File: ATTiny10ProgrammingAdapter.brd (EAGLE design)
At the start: 46.7 x 45.7 mm, 9 parts

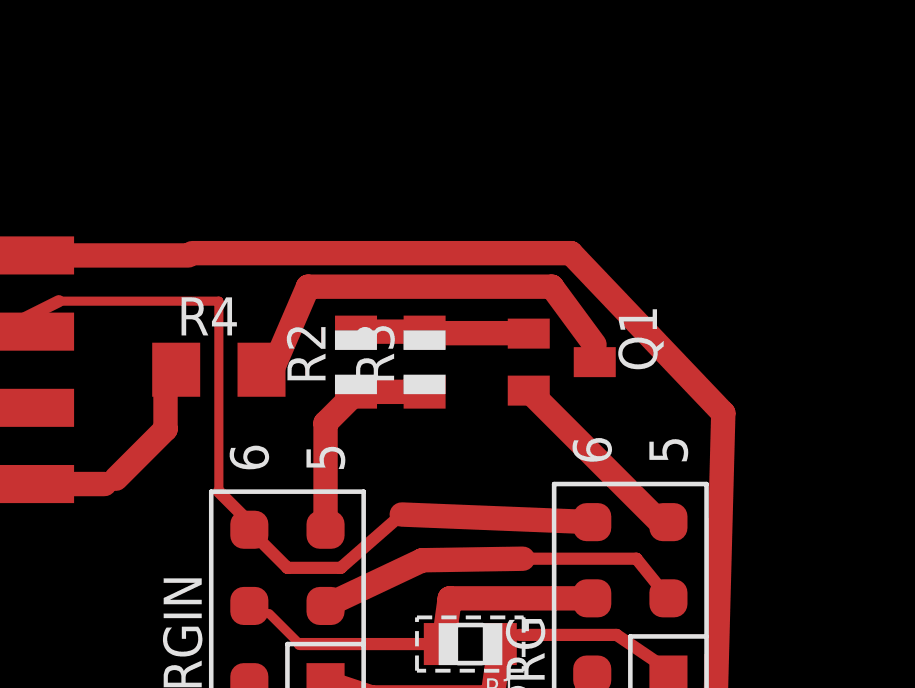
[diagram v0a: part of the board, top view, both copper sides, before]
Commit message: Fix rest to default to pulldown when not active
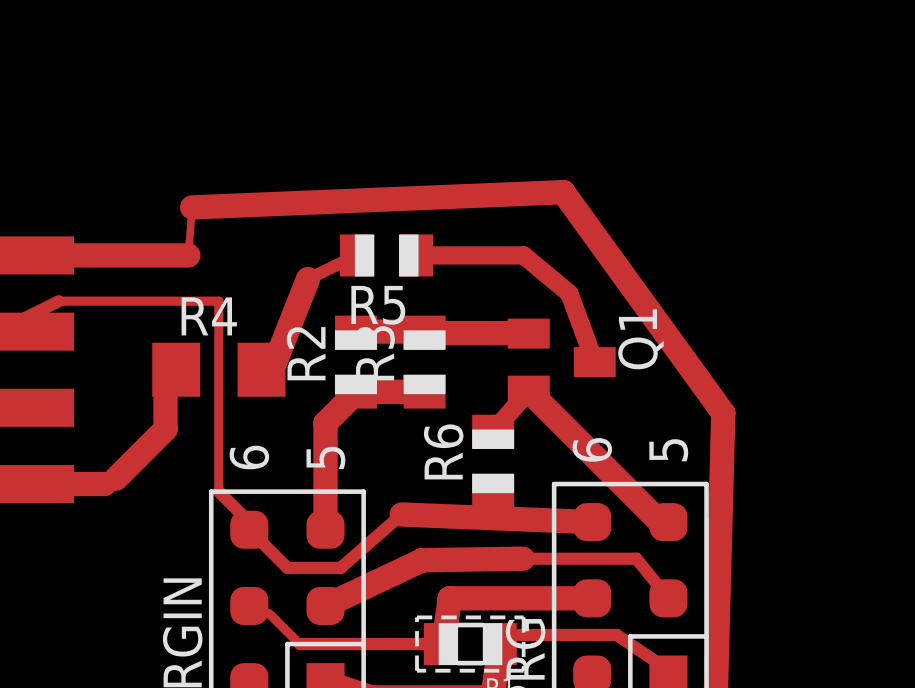
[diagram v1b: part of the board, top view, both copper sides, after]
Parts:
- added R5: 50k, adafruit:R0805
- added R6: 2k, adafruit:R0805
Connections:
- new net N$4: Q1.3, R5.1
- net +12V: now also R5.2; no longer Q1.3
- net GND: now also R6.1
- net RST: now also R6.2
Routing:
- net +12V: track 23.0 -> 13.9 mm
- net N$4: track 0.00 -> 7.99 mm
- net VDD: track 40.7 -> 43.6 mm
- net RST: track 6.47 -> 8.25 mm
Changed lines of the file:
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@@
 <element name="PRGIN" library="LL" package="HEADER_PRG_2X03_ETCH" value="CON_HEADER_PRG_AVR_ICSP_ETCH" x="12.192" y="9.652" rot="R90"/>
 <element name="R4" library="LL" package="R1206" value="0" x="9.906" y="17.526"/>
+<element name="R5" library="adafruit" package="R0805" value="50k" x="15.494" y="21.336" rot="R180"/>
+<element name="R6" library="adafruit" package="R0805" value="2k" x="19.05" y="14.478" rot="R90"/>
 </elements>
 <signals>
 <signal name="RST">
-<contactref element="Q1" pad="2"/>
 <contactref element="PRG" pad="5"/>
 <wire x1="24.6126" y1="12.446" x2="24.892" y2="12.446" width="0.254" layer="1"/>
 <wire x1="20.2438" y1="16.8148" x2="24.6126" y2="12.446" width="0.8128" layer="1"/>
-<wire x1="20.2438" y1="16.8148" x2="20.236" y2="16.83" width="0.254" layer="1"/>
+<contactref element="R6" pad="2"/>
+<contactref element="Q1" pad="2"/>
+<wire x1="20.2438" y1="16.8148" x2="19.05" y2="15.478" width="0.6096" layer="1"/>
+<wire x1="20.2438" y1="16.8148" x2="20.236" y2="16.83" width="0" layer="19" extent="1-1"/>
 </signal>
 <signal name="TPICLK">
@@
 <wire x1="9.906" y1="19.812" x2="4.572" y2="19.812" width="0.3048" layer="1"/>
 <wire x1="4.572" y1="19.812" x2="2.54" y2="18.796" width="0.4064" layer="1"/>
+<contactref element="R6" pad="1"/>
 </signal>
 <signal name="+12V">
 <contactref element="EXTPOWER" pad="4"/>
-<contactref element="Q1" pad="3"/>
 <wire x1="2.54" y1="13.716" x2="6.096" y2="13.716" width="0.8128" layer="1"/>
-<wire x1="22.4282" y1="18.3642" x2="22.4282" y2="17.78" width="0.254" layer="1"/>
-<wire x1="21.0058" y1="20.2946" x2="22.4282" y2="18.3642" width="0.8128" layer="1"/>
-<wire x1="12.8778" y1="20.2946" x2="21.0058" y2="20.2946" width="0.8128" layer="1"/>
 <wire x1="6.477" y1="13.8938" x2="8.128" y2="15.5448" width="0.8128" layer="1"/>
 <wire x1="8.128" y1="15.5448" x2="8.128" y2="17.272" width="0.8128" layer="1"/>
 <wire x1="8.128" y1="17.272" x2="8.382" y2="17.526" width="0.254" layer="1"/>
-<wire x1="11.684" y1="17.526" x2="12.8778" y2="20.2946" width="0.8128" layer="1"/>
-<wire x1="22.4282" y1="17.78" x2="22.436" y2="17.78" width="0.254" layer="1"/>
+<wire x1="11.684" y1="17.526" x2="12.8778" y2="20.5486" width="0.8128" layer="1"/>
 <wire x1="6.477" y1="13.8938" x2="6.096" y2="13.716" width="0.254" layer="1"/>
 <contactref element="R4" pad="1"/>
@@
 <wire x1="8.382" y1="17.526" x2="8.484" y2="17.526" width="0.4064" layer="1"/>
 <wire x1="11.684" y1="17.526" x2="11.328" y2="17.526" width="0.4064" layer="1"/>
+<contactref element="R5" pad="2"/>
+<wire x1="14.494" y1="21.336" x2="12.8778" y2="20.5486" width="0.4064" layer="1"/>
 <wire x1="8.484" y1="17.526" x2="11.328" y2="17.526" width="0" layer="19" extent="1-1"/>
 </signal>
@@
 <wire x1="26.4668" y1="6.5278" x2="23.876" y2="3.683" width="0.8128" layer="1"/>
 <wire x1="26.7208" y1="16.0782" x2="26.4668" y2="6.5278" width="0.8128" layer="1"/>
-<wire x1="21.6408" y1="21.4122" x2="26.7208" y2="16.0782" width="0.8128" layer="1"/>
-<wire x1="9.017" y1="21.4122" x2="21.6408" y2="21.4122" width="0.8128" layer="1"/>
-<wire x1="9.017" y1="21.4122" x2="8.89" y2="21.336" width="0.254" layer="1"/>
+<wire x1="21.3868" y1="23.4442" x2="26.7208" y2="16.0782" width="0.8128" layer="1"/>
+<wire x1="9.017" y1="22.9362" x2="21.3868" y2="23.4442" width="0.8128" layer="1"/>
+<wire x1="9.017" y1="22.9362" x2="8.89" y2="21.336" width="0.254" layer="1"/>
 </signal>
 <signal name="N$1">
@@
 </polygon>
 </signal>
+<signal name="N$4">
+<contactref element="Q1" pad="3"/>
+<contactref element="R5" pad="1"/>
+<wire x1="22.436" y1="17.78" x2="21.59" y2="20.066" width="0.6096" layer="1"/>
+<wire x1="21.59" y1="20.066" x2="20.066" y2="21.336" width="0.6096" layer="1"/>
+<wire x1="20.066" y1="21.336" x2="16.494" y2="21.336" width="0.6096" layer="1"/>
+</signal>
 </signals>

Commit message: Tune traces
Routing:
- net GND: track 28.3 -> 27.6 mm
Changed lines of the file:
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@@
 </class>
 </classes>
-<designrules name="ll-etch *">
+<designrules name="ll-etch-lax">
 <description language="de">&lt;b&gt;EAGLE Design Rules&lt;/b&gt;
 &lt;p&gt;
@@
 <description language="en">&lt;b&gt;LL's Etch Rules&lt;/b&gt;
 &lt;p&gt;
-Toner transfer etch tuned DRU</description>
+Toner transfer etch tuned DRU
+(Most lax version designed to allow 8mil traces between 0805s and 0603s to even exist</description>
 <param name="layerSetup" value="(1*16)"/>
 <param name="mtCopper" value="0.0356mm 0.0356mm 0.0356mm 0.0356mm 0.0356mm 0.0356mm 0.0356mm 0.0356mm 0.0356mm 0.0356mm 0.0356mm 0.0356mm 0.0356mm 0.0356mm 0.0356mm 0.0356mm"/>
 <param name="mtIsolate" value="1.5011mm 0.1499mm 0.2007mm 0.1499mm 0.2007mm 0.1499mm 0.2007mm 0.1499mm 0.2007mm 0.1499mm 0.2007mm 0.1499mm 0.2007mm 0.1499mm 0.2007mm"/>
 <param name="mdWireWire" value="8mil"/>
-<param name="mdWirePad" value="12mil"/>
+<param name="mdWirePad" value="7mil"/>
 <param name="mdWireVia" value="12mil"/>
-<param name="mdPadPad" value="18mil"/>
+<param name="mdPadPad" value="12mil"/>
 <param name="mdPadVia" value="18mil"/>
 <param name="mdViaVia" value="20mil"/>
@@
 <param name="mdDrill" value="30mil"/>
 <param name="mdSmdStop" value="0mil"/>
-<param name="msWidth" value="10mil"/>
+<param name="msWidth" value="8mil"/>
 <param name="msDrill" value="21mil"/>
 <param name="msMicroVia" value="21mil"/>
@@
 <wire x1="10.922" y1="12.192" x2="10.922" y2="12.446" width="0.3048" layer="1"/>
 <wire x1="10.922" y1="12.446" x2="9.906" y2="13.462" width="0.4064" layer="1"/>
-<wire x1="9.906" y1="13.462" x2="9.906" y2="19.812" width="0.3048" layer="1"/>
-<wire x1="9.906" y1="19.812" x2="4.572" y2="19.812" width="0.3048" layer="1"/>
-<wire x1="4.572" y1="19.812" x2="2.54" y2="18.796" width="0.4064" layer="1"/>
+<wire x1="9.906" y1="13.462" x2="9.906" y2="16.002" width="0.6096" layer="1"/>
+<wire x1="9.906" y1="16.002" x2="9.906" y2="19.304" width="0.3048" layer="1"/>
+<wire x1="9.906" y1="19.304" x2="6.096" y2="19.304" width="0.6096" layer="1"/>
+<wire x1="6.096" y1="19.304" x2="4.826" y2="18.796" width="0.6096" layer="1"/>
+<wire x1="4.826" y1="18.796" x2="2.54" y2="18.796" width="0.4064" layer="1"/>
 <contactref element="R6" pad="1"/>
 </signal>
@@
 <wire x1="11.684" y1="17.526" x2="11.328" y2="17.526" width="0.4064" layer="1"/>
 <contactref element="R5" pad="2"/>
-<wire x1="14.494" y1="21.336" x2="12.8778" y2="20.5486" width="0.4064" layer="1"/>
+<wire x1="14.494" y1="21.336" x2="12.8778" y2="20.5486" width="0.6096" layer="1"/>
 <wire x1="8.484" y1="17.526" x2="11.328" y2="17.526" width="0" layer="19" extent="1-1"/>
 </signal>
@@
 <wire x1="21.3868" y1="23.4442" x2="26.7208" y2="16.0782" width="0.8128" layer="1"/>
 <wire x1="9.017" y1="22.9362" x2="21.3868" y2="23.4442" width="0.8128" layer="1"/>
-<wire x1="9.017" y1="22.9362" x2="8.89" y2="21.336" width="0.254" layer="1"/>
+<wire x1="9.017" y1="22.9362" x2="8.89" y2="21.336" width="0.6096" layer="1"/>
 </signal>
 <signal name="N$1">
@@
 </signal>
 </signals>
+<errors>
+</errors>
 </board>
 </drawing>

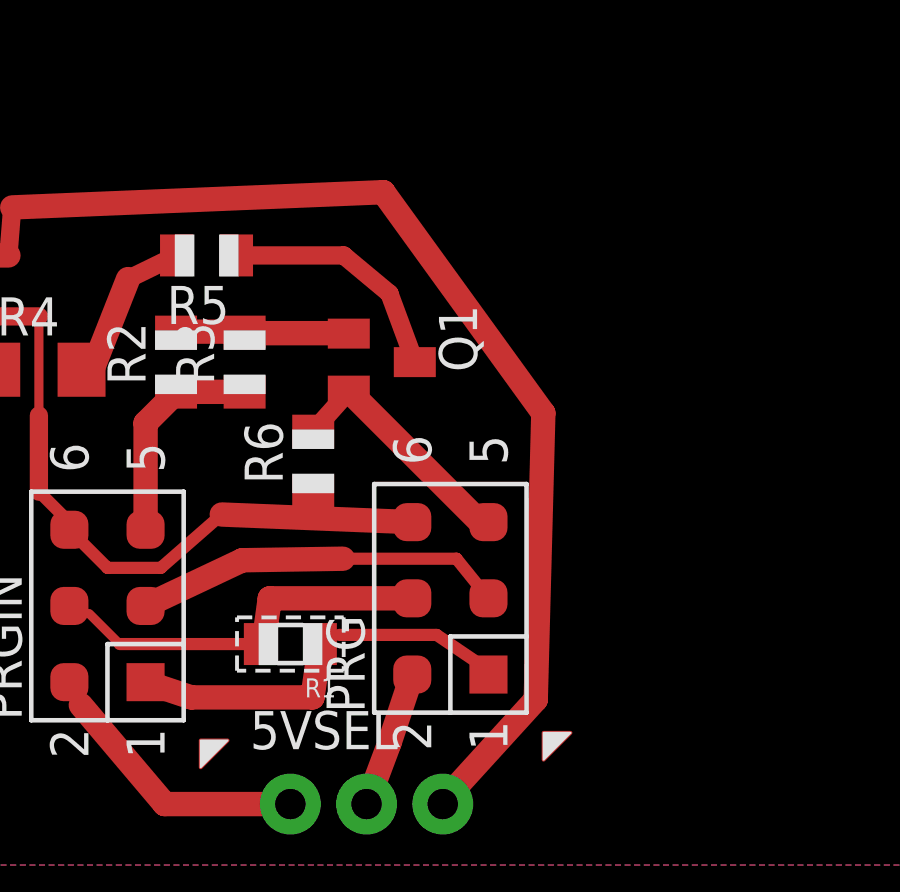
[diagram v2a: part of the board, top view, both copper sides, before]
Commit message: Add reset pullup to VDD
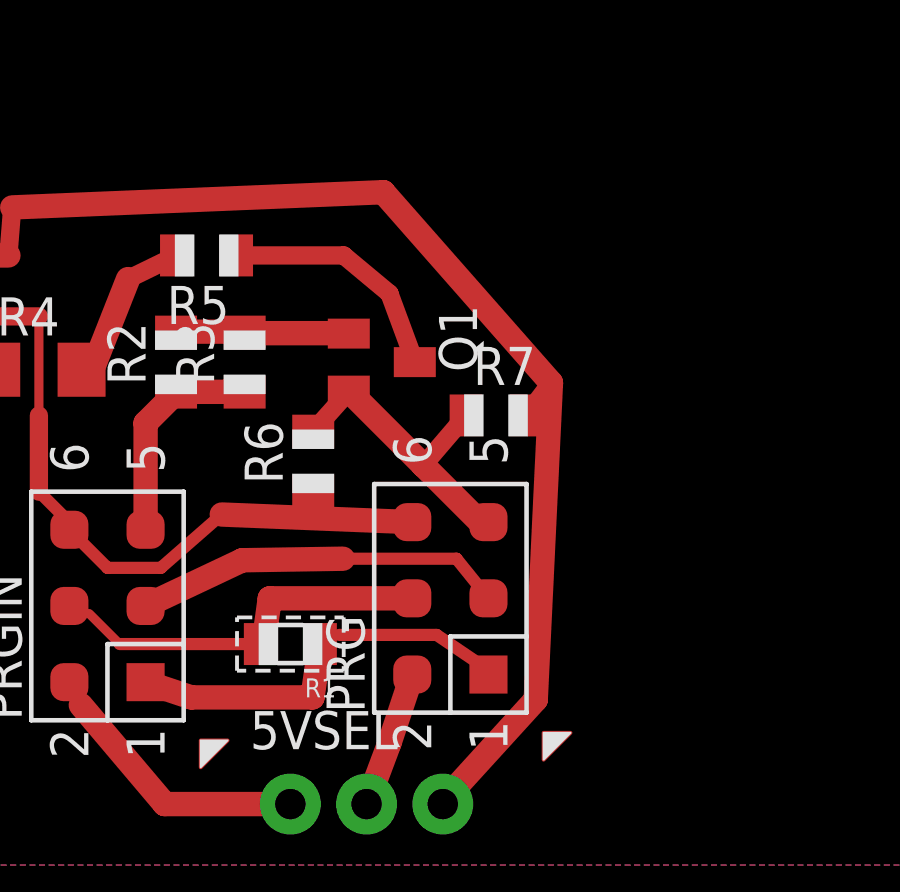
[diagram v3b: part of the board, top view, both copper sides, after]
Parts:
- added R7: 2k, adafruit:R0805
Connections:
- net RST: now also R7.1
- net VDD: now also R7.2
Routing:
- net RST: track 8.25 -> 10.4 mm
- net VDD: track 43.6 -> 45.4 mm
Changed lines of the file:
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@@
 <element name="R5" library="adafruit" package="R0805" value="50k" x="15.494" y="21.336" rot="R180"/>
 <element name="R6" library="adafruit" package="R0805" value="2k" x="19.05" y="14.478" rot="R90"/>
+<element name="R7" library="adafruit" package="R0805" value="2k" x="25.146" y="16.002"/>
 </elements>
 <signals>
@@
 <contactref element="PRG" pad="5"/>
 <wire x1="24.6126" y1="12.446" x2="24.892" y2="12.446" width="0.254" layer="1"/>
-<wire x1="20.2438" y1="16.8148" x2="24.6126" y2="12.446" width="0.8128" layer="1"/>
+<wire x1="20.2438" y1="16.8148" x2="22.7203" y2="14.3383" width="0.8128" layer="1"/>
 <contactref element="R6" pad="2"/>
 <contactref element="Q1" pad="2"/>
+<wire x1="22.7203" y1="14.3383" x2="24.6126" y2="12.446" width="0.8128" layer="1"/>
 <wire x1="20.2438" y1="16.8148" x2="19.05" y2="15.478" width="0.6096" layer="1"/>
+<contactref element="R7" pad="1"/>
+<wire x1="24.146" y1="16.002" x2="22.7203" y2="14.3383" width="0.6096" layer="1"/>
 <wire x1="20.2438" y1="16.8148" x2="20.236" y2="16.83" width="0" layer="19" extent="1-1"/>
 </signal>
@@
 <wire x1="23.876" y1="3.683" x2="23.368" y2="3.048" width="0.254" layer="1"/>
 <wire x1="26.4668" y1="6.5278" x2="23.876" y2="3.683" width="0.8128" layer="1"/>
-<wire x1="26.7208" y1="16.0782" x2="26.4668" y2="6.5278" width="0.8128" layer="1"/>
-<wire x1="21.3868" y1="23.4442" x2="26.7208" y2="16.0782" width="0.8128" layer="1"/>
+<wire x1="26.9748" y1="17.0942" x2="26.4668" y2="6.5278" width="0.8128" layer="1"/>
+<wire x1="21.3868" y1="23.4442" x2="26.9748" y2="17.0942" width="0.8128" layer="1"/>
 <wire x1="9.017" y1="22.9362" x2="21.3868" y2="23.4442" width="0.8128" layer="1"/>
 <wire x1="9.017" y1="22.9362" x2="8.89" y2="21.336" width="0.6096" layer="1"/>
+<contactref element="R7" pad="2"/>
+<wire x1="26.9748" y1="17.0942" x2="26.146" y2="16.002" width="0.6096" layer="1"/>
 </signal>
 <signal name="N$1">
@@
 </signal>
 </signals>
-<errors>
-</errors>
 </board>
 </drawing>

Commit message: Tune up boards for printing
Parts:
- added U$1: (no value), LL:L2LOGO
- moved EXTPOWER 16.5 mm to (7.37, 33.3), turned to 180 degrees
- moved R1 6.25 mm to (12.7, 11.2)
- moved R4 6.25 mm to (4.32, 20.3)
- moved R7 6.25 mm to (19.6, 18.8)
- moved PRGIN 6.25 mm to (6.60, 12.4)
- moved 5VSEL 6.25 mm to (15.2, 5.84)
- moved PRG 6.25 mm to (18.0, 12.7)
- moved Q1 6.25 mm to (15.7, 20.6)
- moved R2 6.25 mm to (8.89, 20.6)
- moved R3 6.25 mm to (11.2, 20.6)
- moved R5 6.25 mm to (9.91, 24.1)
- moved R6 6.25 mm to (13.5, 17.3)
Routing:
- net VDD: track 45.4 -> 35.4 mm
- net +12V: track 13.9 -> 20.0 mm
- net GND: track 27.6 -> 33.0 mm
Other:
- board size 46.7 x 45.7 mm -> 25.6 x 35.8 mm
- board text added: "ATTiny Prog Adapter 2013-3-24"
